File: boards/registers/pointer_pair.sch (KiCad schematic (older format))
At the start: 7 parts, among them U5 74ACT86, U6 74ACT08, U7 74ACT32, U8 74ACT32

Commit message: Main board revision 2
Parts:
- added unit 4 of U5
- added unit 3 of U6
- added unit 4 of U6
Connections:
- net GND: now also U5.12, U5.13, U6.10, U6.12, U6.13, U6.9
- no-connect marks 0 -> 3
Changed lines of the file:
@@
 	1    0    0    -1
 $EndComp
+$Comp
+L 74xx:74LS08 U6
+U 3 1 5E396484
+P 9900 950
+F 0 "U6" H 9900 1275 50  0000 C CNN
+F 1 "74ACT08" H 9900 1184 50  0000 C CNN
+F 2 "" H 9900 950 50  0001 C CNN
+F 3 "http://www.ti.com/lit/gpn/sn74LS08" H 9900 950 50  0001 C CNN
+	3    9900 950
+	1    0    0    -1
+$EndComp
+$Comp
+L 74xx:74LS08 U6
+U 4 1 5E39E32D
+P 9900 1500
+F 0 "U6" H 9900 1825 50  0000 C CNN
+F 1 "74ACT08" H 9900 1734 50  0000 C CNN
+F 2 "" H 9900 1500 50  0001 C CNN
+F 3 "http://www.ti.com/lit/gpn/sn74LS08" H 9900 1500 50  0001 C CNN
+	4    9900 1500
+	1    0    0    -1
+$EndComp
+$Comp
+L power:GND #PWR0125
+U 1 1 5E3A0364
+P 9600 850
+F 0 "#PWR0125" H 9600 600 50  0001 C CNN
+F 1 "GND" H 9605 677 50  0000 C CNN
+F 2 "" H 9600 850 50  0001 C CNN
+F 3 "" H 9600 850 50  0001 C CNN
+	1    9600 850
+	0    1    1    0
+$EndComp
+$Comp
+L power:GND #PWR0130
+U 1 1 5E3A1055
+P 9600 1050
+F 0 "#PWR0130" H 9600 800 50  0001 C CNN
+F 1 "GND" H 9605 877 50  0000 C CNN
+F 2 "" H 9600 1050 50  0001 C CNN
+F 3 "" H 9600 1050 50  0001 C CNN
+	1    9600 1050
+	0    1    1    0
+$EndComp
+$Comp
+L power:GND #PWR0131
+U 1 1 5E3A133D
+P 9600 1400
+F 0 "#PWR0131" H 9600 1150 50  0001 C CNN
+F 1 "GND" H 9605 1227 50  0000 C CNN
+F 2 "" H 9600 1400 50  0001 C CNN
+F 3 "" H 9600 1400 50  0001 C CNN
+	1    9600 1400
+	0    1    1    0
+$EndComp
+$Comp
+L power:GND #PWR0132
+U 1 1 5E3A1801
+P 9600 1600
+F 0 "#PWR0132" H 9600 1350 50  0001 C CNN
+F 1 "GND" H 9605 1427 50  0000 C CNN
+F 2 "" H 9600 1600 50  0001 C CNN
+F 3 "" H 9600 1600 50  0001 C CNN
+	1    9600 1600
+	0    1    1    0
+$EndComp
+NoConn ~ 10200 950
+NoConn ~ 10200 1500
+$Comp
+L 74xx:74LS86 U5
+U 4 1 5E3DCDDF
+P 9900 2050
+F 0 "U5" H 9900 2375 50  0000 C CNN
+F 1 "74ACT86" H 9900 2284 50  0000 C CNN
+F 2 "" H 9900 2050 50  0001 C CNN
+F 3 "74xx/74ls86.pdf" H 9900 2050 50  0001 C CNN
+	4    9900 2050
+	1    0    0    -1
+$EndComp
+$Comp
+L power:GND #PWR?
+U 1 1 5E3E1729
+P 9600 2150
+F 0 "#PWR?" H 9600 1900 50  0001 C CNN
+F 1 "GND" H 9605 1977 50  0000 C CNN
+F 2 "" H 9600 2150 50  0001 C CNN
+F 3 "" H 9600 2150 50  0001 C CNN
+	1    9600 2150
+	0    1    1    0
+$EndComp
+$Comp
+L power:GND #PWR?
+U 1 1 5E3E1AD3
+P 9600 1950
+F 0 "#PWR?" H 9600 1700 50  0001 C CNN
+F 1 "GND" H 9605 1777 50  0000 C CNN
+F 2 "" H 9600 1950 50  0001 C CNN
+F 3 "" H 9600 1950 50  0001 C CNN
+	1    9600 1950
+	0    1    1    0
+$EndComp
+NoConn ~ 10200 2050
 $EndSCHEMATC

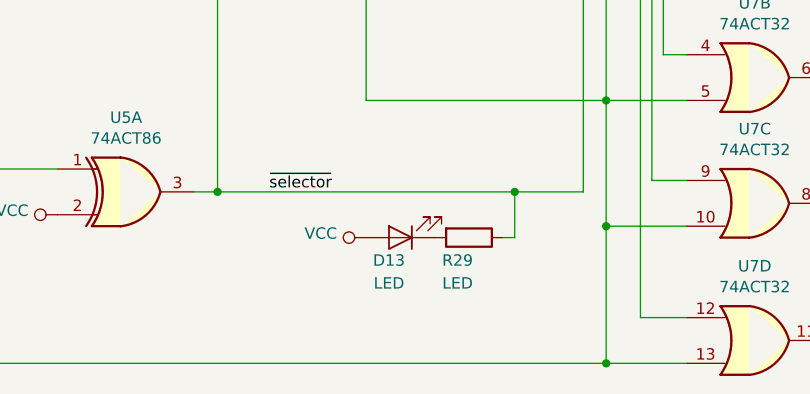
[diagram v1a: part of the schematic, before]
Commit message: LEDs and LED resistors
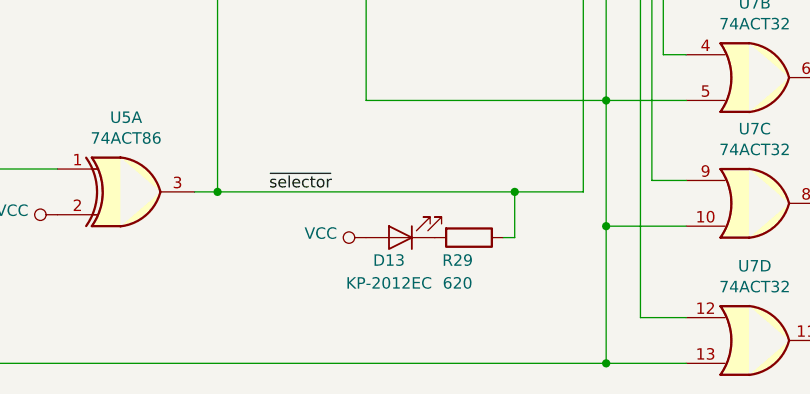
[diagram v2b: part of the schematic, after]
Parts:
- D13: value LED -> KP-2012EC
- R29: value LED -> 620
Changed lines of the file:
@@
 P 3900 6600
 F 0 "D13" H 3950 6700 50  0000 C CNN
-F 1 "LED" H 3950 6800 50  0000 C CNN
+F 1 "KP-2012EC" H 3950 6800 50  0000 C CNN
 F 2 "LED_SMD:LED_0805_2012Metric" H 3900 6600 50  0001 C CNN
 F 3 "~" H 3900 6600 50  0001 C CNN
@@
 P 4200 6600
 F 0 "R29" V 4300 6550 50  0000 C CNN
-F 1 "LED" V 4400 6550 50  0000 C CNN
+F 1 "620" V 4400 6550 50  0000 C CNN
 F 2 "Resistor_SMD:R_0805_2012Metric" V 4130 6600 50  0001 C CNN
 F 3 "~" H 4200 6600 50  0001 C CNN

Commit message: Part names
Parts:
- U5: value 74ACT86 -> MC74ACT86DG
- U6: value 74ACT08 -> SN74ACT08PW
- U7, U8: value 74ACT32 -> SN74ACT32PWR
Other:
- moved on the sheet: U5E, U6E, U8E
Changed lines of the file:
@@
 P 5450 5350
 F 0 "U7" H 5450 5675 50  0000 C CNN
-F 1 "74ACT32" H 5450 5584 50  0000 C CNN
+F 1 "SN74ACT32PWR" H 5450 5584 50  0000 C CNN
 F 2 "Package_SO:TSSOP-14_4.4x5mm_P0.65mm" H 5450 5350 50  0001 C CNN
 F 3 "http://www.ti.com/lit/gpn/sn74LS32" H 5450 5350 50  0001 C CNN
@@
 P 5450 5900
 F 0 "U7" H 5450 6225 50  0000 C CNN
-F 1 "74ACT32" H 5450 6134 50  0000 C CNN
+F 1 "SN74ACT32PWR" H 5450 6134 50  0000 C CNN
 F 2 "Package_SO:TSSOP-14_4.4x5mm_P0.65mm" H 5450 5900 50  0001 C CNN
 F 3 "http://www.ti.com/lit/gpn/sn74LS32" H 5450 5900 50  0001 C CNN
@@
 P 5450 6450
 F 0 "U7" H 5450 6775 50  0000 C CNN
-F 1 "74ACT32" H 5450 6684 50  0000 C CNN
+F 1 "SN74ACT32PWR" H 5450 6684 50  0000 C CNN
 F 2 "Package_SO:TSSOP-14_4.4x5mm_P0.65mm" H 5450 6450 50  0001 C CNN
 F 3 "http://www.ti.com/lit/gpn/sn74LS32" H 5450 6450 50  0001 C CNN
@@
 P 5450 7050
 F 0 "U7" H 5450 7375 50  0000 C CNN
-F 1 "74ACT32" H 5450 7284 50  0000 C CNN
+F 1 "SN74ACT32PWR" H 5450 7284 50  0000 C CNN
 F 2 "Package_SO:TSSOP-14_4.4x5mm_P0.65mm" H 5450 7050 50  0001 C CNN
 F 3 "http://www.ti.com/lit/gpn/sn74LS32" H 5450 7050 50  0001 C CNN
@@
 L 74xx:74LS32 U8
 U 5 1 5E5F17C1
-P 9000 4450
-F 0 "U8" H 9230 4496 50  0000 L CNN
-F 1 "74ACT32" H 9230 4405 50  0000 L CNN
-F 2 "Package_SO:TSSOP-14_4.4x5mm_P0.65mm" H 9000 4450 50  0001 C CNN
-F 3 "http://www.ti.com/lit/gpn/sn74LS32" H 9000 4450 50  0001 C CNN
-	5    9000 4450
+P 9850 4450
+F 0 "U8" H 10080 4496 50  0000 L CNN
+F 1 "SN74ACT32PWR" H 10080 4405 50  0000 L CNN
+F 2 "Package_SO:TSSOP-14_4.4x5mm_P0.65mm" H 9850 4450 50  0001 C CNN
+F 3 "http://www.ti.com/lit/gpn/sn74LS32" H 9850 4450 50  0001 C CNN
+	5    9850 4450
 	1    0    0    -1
 $EndComp
@@
 P 5500 2250
 F 0 "U8" H 5500 2575 50  0000 C CNN
-F 1 "74ACT32" H 5500 2484 50  0000 C CNN
+F 1 "SN74ACT32PWR" H 5500 2484 50  0000 C CNN
 F 2 "Package_SO:TSSOP-14_4.4x5mm_P0.65mm" H 5500 2250 50  0001 C CNN
 F 3 "http://www.ti.com/lit/gpn/sn74LS32" H 5500 2250 50  0001 C CNN
@@
 P 5500 2800
 F 0 "U8" H 5500 3125 50  0000 C CNN
-F 1 "74ACT32" H 5500 3034 50  0000 C CNN
+F 1 "SN74ACT32PWR" H 5500 3034 50  0000 C CNN
 F 2 "Package_SO:TSSOP-14_4.4x5mm_P0.65mm" H 5500 2800 50  0001 C CNN
 F 3 "http://www.ti.com/lit/gpn/sn74LS32" H 5500 2800 50  0001 C CNN
@@
 P 5500 3350
 F 0 "U8" H 5500 3675 50  0000 C CNN
-F 1 "74ACT32" H 5500 3584 50  0000 C CNN
+F 1 "SN74ACT32PWR" H 5500 3584 50  0000 C CNN
 F 2 "Package_SO:TSSOP-14_4.4x5mm_P0.65mm" H 5500 3350 50  0001 C CNN
 F 3 "http://www.ti.com/lit/gpn/sn74LS32" H 5500 3350 50  0001 C CNN
@@
 P 5500 3950
 F 0 "U8" H 5500 4275 50  0000 C CNN
-F 1 "74ACT32" H 5500 4184 50  0000 C CNN
+F 1 "SN74ACT32PWR" H 5500 4184 50  0000 C CNN
 F 2 "Package_SO:TSSOP-14_4.4x5mm_P0.65mm" H 5500 3950 50  0001 C CNN
 F 3 "http://www.ti.com/lit/gpn/sn74LS32" H 5500 3950 50  0001 C CNN
@@
 L power:GND #PWR047
 U 1 1 5E651ABF
-P 9000 4950
-F 0 "#PWR047" H 9000 4700 50  0001 C CNN
-F 1 "GND" H 9005 4777 50  0000 C CNN
-F 2 "" H 9000 4950 50  0001 C CNN
-F 3 "" H 9000 4950 50  0001 C CNN
-	1    9000 4950
+P 9850 4950
+F 0 "#PWR047" H 9850 4700 50  0001 C CNN
+F 1 "GND" H 9855 4777 50  0000 C CNN
+F 2 "" H 9850 4950 50  0001 C CNN
+F 3 "" H 9850 4950 50  0001 C CNN
+	1    9850 4950
 	1    0    0    -1
 $EndComp
@@
 L power:VCC #PWR046
 U 1 1 5E651F92
-P 9000 3950
-F 0 "#PWR046" H 9000 3800 50  0001 C CNN
-F 1 "VCC" H 9017 4123 50  0000 C CNN
-F 2 "" H 9000 3950 50  0001 C CNN
-F 3 "" H 9000 3950 50  0001 C CNN
-	1    9000 3950
+P 9850 3950
+F 0 "#PWR046" H 9850 3800 50  0001 C CNN
+F 1 "VCC" H 9867 4123 50  0000 C CNN
+F 2 "" H 9850 3950 50  0001 C CNN
+F 3 "" H 9850 3950 50  0001 C CNN
+	1    9850 3950
 	1    0    0    -1
 $EndComp
@@
 P 8250 4450
 F 0 "U7" H 8480 4496 50  0000 L CNN
-F 1 "74ACT32" H 8480 4405 50  0000 L CNN
+F 1 "SN74ACT32PWR" H 8480 4405 50  0000 L CNN
 F 2 "Package_SO:TSSOP-14_4.4x5mm_P0.65mm" H 8250 4450 50  0001 C CNN
 F 3 "http://www.ti.com/lit/gpn/sn74LS32" H 8250 4450 50  0001 C CNN
@@
 P 4000 3150
 F 0 "U6" H 4000 3475 50  0000 C CNN
-F 1 "74ACT08" H 4000 3384 50  0000 C CNN
+F 1 "SN74ACT08PW" H 4000 3384 50  0000 C CNN
 F 2 "Package_SO:TSSOP-14_4.4x5mm_P0.65mm" H 4000 3150 50  0001 C CNN
 F 3 "http://www.ti.com/lit/gpn/sn74LS08" H 4000 3150 50  0001 C CNN
@@
 P 4050 5150
 F 0 "U6" H 4050 5475 50  0000 C CNN
-F 1 "74ACT08" H 4050 5384 50  0000 C CNN
+F 1 "SN74ACT08PW" H 4050 5384 50  0000 C CNN
 F 2 "Package_SO:TSSOP-14_4.4x5mm_P0.65mm" H 4050 5150 50  0001 C CNN
 F 3 "http://www.ti.com/lit/gpn/sn74LS08" H 4050 5150 50  0001 C CNN
@@
 L 74xx:74LS08 U6
 U 5 1 5E6E224D
-P 9750 4450
-F 0 "U6" H 9980 4496 50  0000 L CNN
-F 1 "74ACT08" H 9980 4405 50  0000 L CNN
-F 2 "Package_SO:TSSOP-14_4.4x5mm_P0.65mm" H 9750 4450 50  0001 C CNN
-F 3 "http://www.ti.com/lit/gpn/sn74LS08" H 9750 4450 50  0001 C CNN
-	5    9750 4450
+P 8600 5750
+F 0 "U6" H 8830 5796 50  0000 L CNN
+F 1 "SN74ACT08PW" H 8830 5705 50  0000 L CNN
+F 2 "Package_SO:TSSOP-14_4.4x5mm_P0.65mm" H 8600 5750 50  0001 C CNN
+F 3 "http://www.ti.com/lit/gpn/sn74LS08" H 8600 5750 50  0001 C CNN
+	5    8600 5750
 	1    0    0    -1
 $EndComp
@@
 L power:GND #PWR051
 U 1 1 5E6E9084
-P 9750 4950
-F 0 "#PWR051" H 9750 4700 50  0001 C CNN
-F 1 "GND" H 9755 4777 50  0000 C CNN
-F 2 "" H 9750 4950 50  0001 C CNN
-F 3 "" H 9750 4950 50  0001 C CNN
-	1    9750 4950
+P 8600 6250
+F 0 "#PWR051" H 8600 6000 50  0001 C CNN
+F 1 "GND" H 8605 6077 50  0000 C CNN
+F 2 "" H 8600 6250 50  0001 C CNN
+F 3 "" H 8600 6250 50  0001 C CNN
+	1    8600 6250
 	1    0    0    -1
 $EndComp
@@
 L power:VCC #PWR050
 U 1 1 5E6E935B
-P 9750 3950
-F 0 "#PWR050" H 9750 3800 50  0001 C CNN
-F 1 "VCC" H 9767 4123 50  0000 C CNN
-F 2 "" H 9750 3950 50  0001 C CNN
-F 3 "" H 9750 3950 50  0001 C CNN
-	1    9750 3950
+P 8600 5250
+F 0 "#PWR050" H 8600 5100 50  0001 C CNN
+F 1 "VCC" H 8617 5423 50  0000 C CNN
+F 2 "" H 8600 5250 50  0001 C CNN
+F 3 "" H 8600 5250 50  0001 C CNN
+	1    8600 5250
 	1    0    0    -1
 $EndComp
@@
 P 2700 6400
 F 0 "U5" H 2700 6725 50  0000 C CNN
-F 1 "74ACT86" H 2700 6634 50  0000 C CNN
+F 1 "MC74ACT86DG" H 2700 6634 50  0000 C CNN
 F 2 "Package_SO:SOIC-14_3.9x8.7mm_P1.27mm" H 2700 6400 50  0001 C CNN
 F 3 "http://www.ti.com/lit/gpn/sn74HC86" H 2700 6400 50  0001 C CNN
@@
 P 2650 3850
 F 0 "U5" H 2650 4175 50  0000 C CNN
-F 1 "74ACT86" H 2650 4084 50  0000 C CNN
+F 1 "MC74ACT86DG" H 2650 4084 50  0000 C CNN
 F 2 "Package_SO:SOIC-14_3.9x8.7mm_P1.27mm" H 2650 3850 50  0001 C CNN
 F 3 "http://www.ti.com/lit/gpn/sn74HC86" H 2650 3850 50  0001 C CNN
@@
 P 2650 4550
 F 0 "U5" H 2650 4875 50  0000 C CNN
-F 1 "74ACT86" H 2650 4784 50  0000 C CNN
+F 1 "MC74ACT86DG" H 2650 4784 50  0000 C CNN
 F 2 "Package_SO:SOIC-14_3.9x8.7mm_P1.27mm" H 2650 4550 50  0001 C CNN
 F 3 "http://www.ti.com/lit/gpn/sn74HC86" H 2650 4550 50  0001 C CNN
@@
 L 74xx:74HC86 U5
 U 5 1 5EBF0254
-P 10550 4450
-F 0 "U5" H 10780 4496 50  0000 L CNN
-F 1 "74ACT86" H 10780 4405 50  0000 L CNN
-F 2 "Package_SO:SOIC-14_3.9x8.7mm_P1.27mm" H 10550 4450 50  0001 C CNN
-F 3 "http://www.ti.com/lit/gpn/sn74HC86" H 10550 4450 50  0001 C CNN
-	5    10550 4450
+P 9650 5750
+F 0 "U5" H 9880 5796 50  0000 L CNN
+F 1 "MC74ACT86DG" H 9880 5705 50  0000 L CNN
+F 2 "Package_SO:SOIC-14_3.9x8.7mm_P1.27mm" H 9650 5750 50  0001 C CNN
+F 3 "http://www.ti.com/lit/gpn/sn74HC86" H 9650 5750 50  0001 C CNN
+	5    9650 5750
 	1    0    0    -1
 $EndComp
@@
 L power:GND #PWR053
 U 1 1 5EBFF603
-P 10550 4950
-F 0 "#PWR053" H 10550 4700 50  0001 C CNN
-F 1 "GND" H 10555 4777 50  0000 C CNN
-F 2 "" H 10550 4950 50  0001 C CNN
-F 3 "" H 10550 4950 50  0001 C CNN
-	1    10550 4950
+P 9650 6250
+F 0 "#PWR053" H 9650 6000 50  0001 C CNN
+F 1 "GND" H 9655 6077 50  0000 C CNN
+F 2 "" H 9650 6250 50  0001 C CNN
+F 3 "" H 9650 6250 50  0001 C CNN
+	1    9650 6250
 	1    0    0    -1
 $EndComp
@@
 L power:VCC #PWR052
 U 1 1 5EBFFB61
-P 10550 3950
-F 0 "#PWR052" H 10550 3800 50  0001 C CNN
-F 1 "VCC" H 10567 4123 50  0000 C CNN
-F 2 "" H 10550 3950 50  0001 C CNN
-F 3 "" H 10550 3950 50  0001 C CNN
-	1    10550 3950
+P 9650 5250
+F 0 "#PWR052" H 9650 5100 50  0001 C CNN
+F 1 "VCC" H 9667 5423 50  0000 C CNN
+F 2 "" H 9650 5250 50  0001 C CNN
+F 3 "" H 9650 5250 50  0001 C CNN
+	1    9650 5250
 	1    0    0    -1
 $EndComp
@@
 P 9900 950
 F 0 "U6" H 9900 1275 50  0000 C CNN
-F 1 "74ACT08" H 9900 1184 50  0000 C CNN
+F 1 "SN74ACT08PW" H 9900 1184 50  0000 C CNN
 F 2 "" H 9900 950 50  0001 C CNN
 F 3 "http://www.ti.com/lit/gpn/sn74LS08" H 9900 950 50  0001 C CNN
@@
 P 9900 1500
 F 0 "U6" H 9900 1825 50  0000 C CNN
-F 1 "74ACT08" H 9900 1734 50  0000 C CNN
+F 1 "SN74ACT08PW" H 9900 1734 50  0000 C CNN
 F 2 "" H 9900 1500 50  0001 C CNN
 F 3 "http://www.ti.com/lit/gpn/sn74LS08" H 9900 1500 50  0001 C CNN
@@
 P 9900 2050
 F 0 "U5" H 9900 2375 50  0000 C CNN
-F 1 "74ACT86" H 9900 2284 50  0000 C CNN
+F 1 "MC74ACT86DG" H 9900 2284 50  0000 C CNN
 F 2 "" H 9900 2050 50  0001 C CNN
 F 3 "74xx/74ls86.pdf" H 9900 2050 50  0001 C CNN
@@
 $EndComp
 $Comp
-L power:GND #PWR?
+L power:GND #PWR0133
 U 1 1 5E3E1729
 P 9600 2150
-F 0 "#PWR?" H 9600 1900 50  0001 C CNN
+F 0 "#PWR0133" H 9600 1900 50  0001 C CNN
 F 1 "GND" H 9605 1977 50  0000 C CNN
 F 2 "" H 9600 2150 50  0001 C CNN
@@
 $EndComp
 $Comp
-L power:GND #PWR?
+L power:GND #PWR0138
 U 1 1 5E3E1AD3
 P 9600 1950
-F 0 "#PWR?" H 9600 1700 50  0001 C CNN
+F 0 "#PWR0138" H 9600 1700 50  0001 C CNN
 F 1 "GND" H 9605 1777 50  0000 C CNN
 F 2 "" H 9600 1950 50  0001 C CNN

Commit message: Power connector on the IO board
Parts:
- U5: footprint (none) -> Package_SO:SOIC-14_3.9x8.7mm_P1.27mm
- U6: footprint (none) -> Package_SO:TSSOP-14_4.4x5mm_P0.65mm
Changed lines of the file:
@@
 F 0 "U6" H 9900 1275 50  0000 C CNN
 F 1 "SN74ACT08PW" H 9900 1184 50  0000 C CNN
-F 2 "" H 9900 950 50  0001 C CNN
+F 2 "Package_SO:TSSOP-14_4.4x5mm_P0.65mm" H 9900 950 50  0001 C CNN
 F 3 "http://www.ti.com/lit/gpn/sn74LS08" H 9900 950 50  0001 C CNN
 	3    9900 950
@@
 F 0 "U6" H 9900 1825 50  0000 C CNN
 F 1 "SN74ACT08PW" H 9900 1734 50  0000 C CNN
-F 2 "" H 9900 1500 50  0001 C CNN
+F 2 "Package_SO:TSSOP-14_4.4x5mm_P0.65mm" H 9900 1500 50  0001 C CNN
 F 3 "http://www.ti.com/lit/gpn/sn74LS08" H 9900 1500 50  0001 C CNN
 	4    9900 1500
@@
 F 0 "U5" H 9900 2375 50  0000 C CNN
 F 1 "MC74ACT86DG" H 9900 2284 50  0000 C CNN
-F 2 "" H 9900 2050 50  0001 C CNN
+F 2 "Package_SO:SOIC-14_3.9x8.7mm_P1.27mm" H 9900 2050 50  0001 C CNN
 F 3 "74xx/74ls86.pdf" H 9900 2050 50  0001 C CNN
 	4    9900 2050

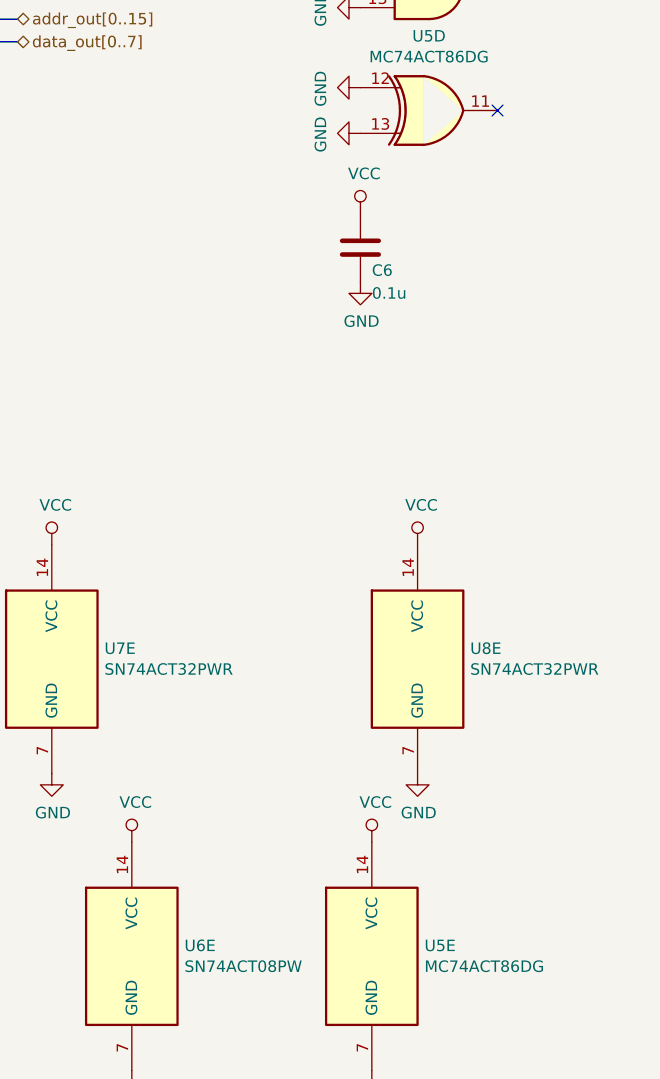
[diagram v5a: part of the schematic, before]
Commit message: Registers: more decoupling capacitors
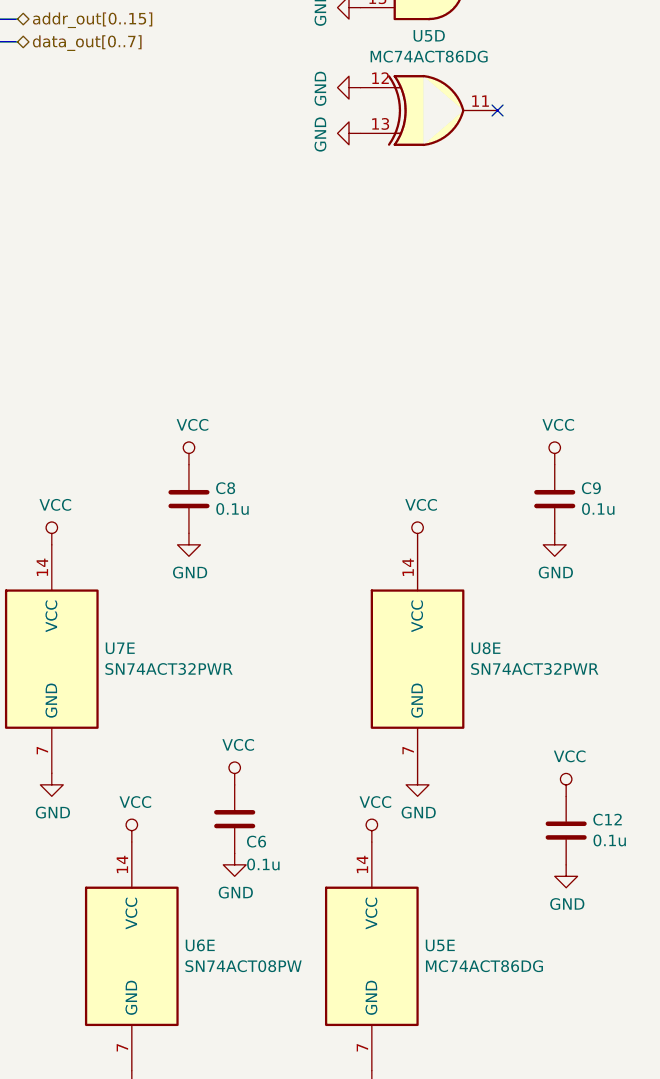
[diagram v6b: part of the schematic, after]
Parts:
- added C12, C8, C9: 0.1u, Capacitor_SMD:C_0805_2012Metric, symbol Device:C
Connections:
- net GND: now also C12.2, C8.2, C9.2
- net VCC: now also C12.1, C8.1, C9.1
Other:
- moved on the sheet: C6
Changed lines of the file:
@@
 L Device:C C6
 U 1 1 5E6C2B4E
-P 9600 2650
-F 0 "C6" H 9650 2550 50  0000 L CNN
-F 1 "0.1u" H 9650 2450 50  0000 L CNN
-F 2 "Capacitor_SMD:C_0805_2012Metric" H 9638 2500 50  0001 C CNN
-F 3 "~" H 9600 2650 50  0001 C CNN
-	1    9600 2650
+P 9050 5150
+F 0 "C6" H 9100 5050 50  0000 L CNN
+F 1 "0.1u" H 9100 4950 50  0000 L CNN
+F 2 "Capacitor_SMD:C_0805_2012Metric" H 9088 5000 50  0001 C CNN
+F 3 "~" H 9050 5150 50  0001 C CNN
+	1    9050 5150
 	1    0    0    -1
 $EndComp
@@
 L power:GND #PWR049
 U 1 1 5E6CC7A3
-P 9600 2800
-F 0 "#PWR049" H 9600 2550 50  0001 C CNN
-F 1 "GND" H 9605 2627 50  0000 C CNN
-F 2 "" H 9600 2800 50  0001 C CNN
-F 3 "" H 9600 2800 50  0001 C CNN
-	1    9600 2800
+P 9050 5300
+F 0 "#PWR049" H 9050 5050 50  0001 C CNN
+F 1 "GND" H 9055 5127 50  0000 C CNN
+F 2 "" H 9050 5300 50  0001 C CNN
+F 3 "" H 9050 5300 50  0001 C CNN
+	1    9050 5300
 	1    0    0    -1
 $EndComp
@@
 L power:VCC #PWR048
 U 1 1 5E6CD3AE
-P 9600 2500
-F 0 "#PWR048" H 9600 2350 50  0001 C CNN
-F 1 "VCC" H 9617 2673 50  0000 C CNN
-F 2 "" H 9600 2500 50  0001 C CNN
-F 3 "" H 9600 2500 50  0001 C CNN
-	1    9600 2500
+P 9050 5000
+F 0 "#PWR048" H 9050 4850 50  0001 C CNN
+F 1 "VCC" H 9067 5173 50  0000 C CNN
+F 2 "" H 9050 5000 50  0001 C CNN
+F 3 "" H 9050 5000 50  0001 C CNN
+	1    9050 5000
 	1    0    0    -1
 $EndComp
@@
 $EndComp
 NoConn ~ 10200 2050
+$Comp
+L Device:C C?
+U 1 1 60147917
+P 8850 3750
+AR Path="/60147917" Ref="C?"  Part="1"
+AR Path="/5E0666E8/60147917" Ref="C8"  Part="1"
+F 0 "C8" H 8965 3796 50  0000 L CNN
+F 1 "0.1u" H 8965 3705 50  0000 L CNN
+F 2 "Capacitor_SMD:C_0805_2012Metric" H 8888 3600 50  0001 C CNN
+F 3 "~" H 8850 3750 50  0001 C CNN
+	1    8850 3750
+	1    0    0    -1
+$EndComp
+$Comp
+L power:VCC #PWR?
+U 1 1 6014791D
+P 8850 3600
+AR Path="/6014791D" Ref="#PWR?"  Part="1"
+AR Path="/5E0666E8/6014791D" Ref="#PWR0150"  Part="1"
+F 0 "#PWR0150" H 8850 3450 50  0001 C CNN
+F 1 "VCC" H 8867 3773 50  0000 C CNN
+F 2 "" H 8850 3600 50  0001 C CNN
+F 3 "" H 8850 3600 50  0001 C CNN
+	1    8850 3600
+	1    0    0    -1
+$EndComp
+$Comp
+L power:GND #PWR?
+U 1 1 60147923
+P 8850 3900
+AR Path="/60147923" Ref="#PWR?"  Part="1"
+AR Path="/5E0666E8/60147923" Ref="#PWR0151"  Part="1"
+F 0 "#PWR0151" H 8850 3650 50  0001 C CNN
+F 1 "GND" H 8855 3727 50  0000 C CNN
+F 2 "" H 8850 3900 50  0001 C CNN
+F 3 "" H 8850 3900 50  0001 C CNN
+	1    8850 3900
+	1    0    0    -1
+$EndComp
+$Comp
+L Device:C C?
+U 1 1 6014C4D8
+P 10450 3750
+AR Path="/6014C4D8" Ref="C?"  Part="1"
+AR Path="/5E0666E8/6014C4D8" Ref="C9"  Part="1"
+F 0 "C9" H 10565 3796 50  0000 L CNN
+F 1 "0.1u" H 10565 3705 50  0000 L CNN
+F 2 "Capacitor_SMD:C_0805_2012Metric" H 10488 3600 50  0001 C CNN
+F 3 "~" H 10450 3750 50  0001 C CNN
+	1    10450 3750
+	1    0    0    -1
+$EndComp
+$Comp
+L power:VCC #PWR?
+U 1 1 6014C4DE
+P 10450 3600
+AR Path="/6014C4DE" Ref="#PWR?"  Part="1"
+AR Path="/5E0666E8/6014C4DE" Ref="#PWR0168"  Part="1"
+F 0 "#PWR0168" H 10450 3450 50  0001 C CNN
+F 1 "VCC" H 10467 3773 50  0000 C CNN
+F 2 "" H 10450 3600 50  0001 C CNN
+F 3 "" H 10450 3600 50  0001 C CNN
+	1    10450 3600
+	1    0    0    -1
+$EndComp
+$Comp
+L power:GND #PWR?
+U 1 1 6014C4E4
+P 10450 3900
+AR Path="/6014C4E4" Ref="#PWR?"  Part="1"
+AR Path="/5E0666E8/6014C4E4" Ref="#PWR0169"  Part="1"
+F 0 "#PWR0169" H 10450 3650 50  0001 C CNN
+F 1 "GND" H 10455 3727 50  0000 C CNN
+F 2 "" H 10450 3900 50  0001 C CNN
+F 3 "" H 10450 3900 50  0001 C CNN
+	1    10450 3900
+	1    0    0    -1
+$EndComp
+$Comp
+L Device:C C?
+U 1 1 6015110B
+P 10500 5200
+AR Path="/6015110B" Ref="C?"  Part="1"
+AR Path="/5E0666E8/6015110B" Ref="C12"  Part="1"
+F 0 "C12" H 10615 5246 50  0000 L CNN
+F 1 "0.1u" H 10615 5155 50  0000 L CNN
+F 2 "Capacitor_SMD:C_0805_2012Metric" H 10538 5050 50  0001 C CNN
+F 3 "~" H 10500 5200 50  0001 C CNN
+	1    10500 5200
+	1    0    0    -1
+$EndComp
+$Comp
+L power:VCC #PWR?
+U 1 1 60151111
+P 10500 5050
+AR Path="/60151111" Ref="#PWR?"  Part="1"
+AR Path="/5E0666E8/60151111" Ref="#PWR0188"  Part="1"
+F 0 "#PWR0188" H 10500 4900 50  0001 C CNN
+F 1 "VCC" H 10517 5223 50  0000 C CNN
+F 2 "" H 10500 5050 50  0001 C CNN
+F 3 "" H 10500 5050 50  0001 C CNN
+	1    10500 5050
+	1    0    0    -1
+$EndComp
+$Comp
+L power:GND #PWR?
+U 1 1 60151117
+P 10500 5350
+AR Path="/60151117" Ref="#PWR?"  Part="1"
+AR Path="/5E0666E8/60151117" Ref="#PWR0189"  Part="1"
+F 0 "#PWR0189" H 10500 5100 50  0001 C CNN
+F 1 "GND" H 10505 5177 50  0000 C CNN
+F 2 "" H 10500 5350 50  0001 C CNN
+F 3 "" H 10500 5350 50  0001 C CNN
+	1    10500 5350
+	1    0    0    -1
+$EndComp
 $EndSCHEMATC
